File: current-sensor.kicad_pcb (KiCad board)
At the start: 2 copper layers, 78 x 39.3 mm, 36 parts, among them J1 ‎0197134001‎, J2 ‎0197134001‎, J3 0731000105, J4 Molex_SL_01x02_Male, J5 Molex_SL_01x02_Male, SW1 PN12SHNA03QE, SW2 OS103011MA7QP1, SW3 OS103011MA7QP1, U1 ACS730xLCTR-40AB, U2 AD8616xRM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

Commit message: swap 100kHz and 1kHz bandwidth positions
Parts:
- moved C1 4.00 mm to (148.0, 98.0)
- moved C3 4.00 mm to (144.0, 98.0)
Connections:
- SW3 pad 2: Net-(C1-Pad2) -> Net-(C3-Pad2)
- SW3 pad 4: Net-(C3-Pad2) -> Net-(C1-Pad2)
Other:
- board text added: "Current Sensor r0 G. Keeth github.com/gkeeth/current-sensor 2020-10-17"
- board text removed: "Current Sensor r0 G. Keeth github.com/gkeeth/current-sensor 2020-08-13"

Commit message: update pcb with hall effect sensor PN change
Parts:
- U1: value ACS730xLCTR-40AB -> ACS730xLCTR-20AB

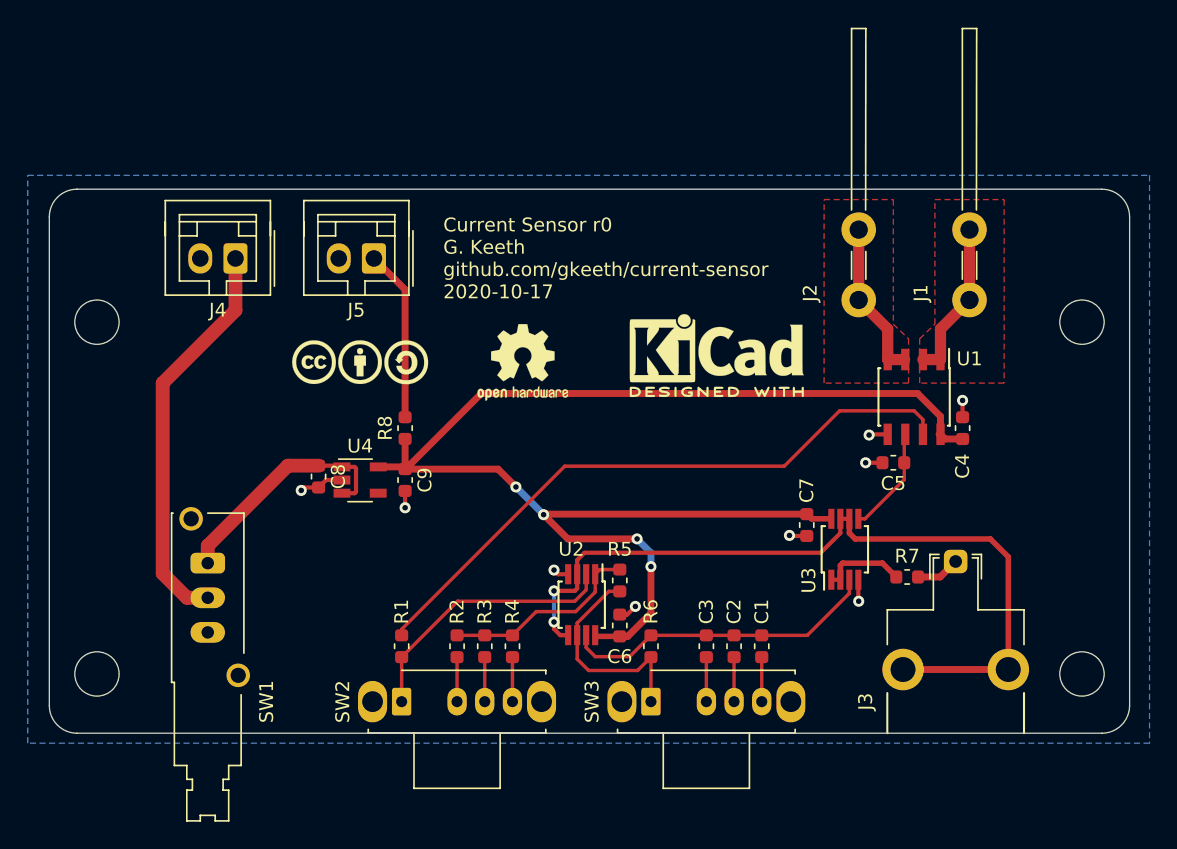
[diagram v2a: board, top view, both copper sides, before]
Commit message: adjust planes around current connectors and add silk
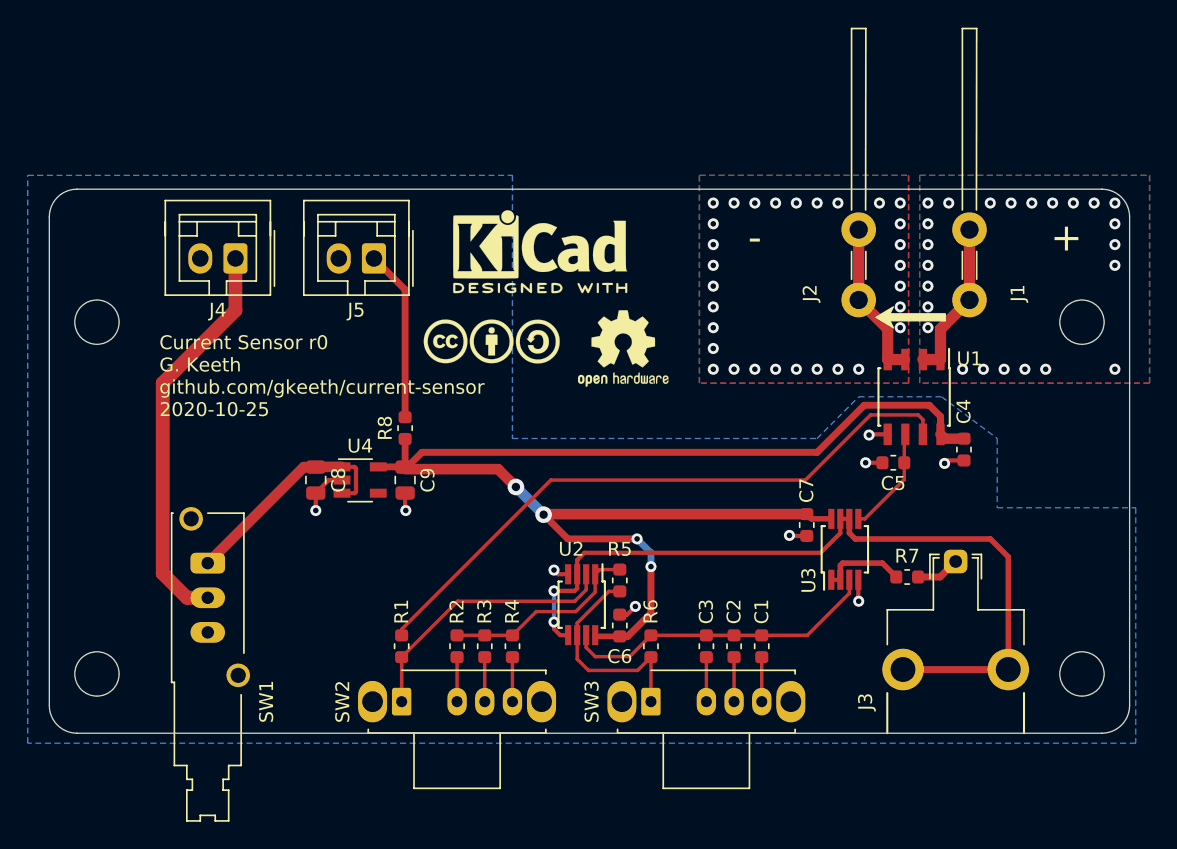
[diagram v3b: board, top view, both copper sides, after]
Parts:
- C8, C9: footprint Capacitor_SMD:C_0603_1608Metric -> Capacitor_SMD:C_0805_2012Metric
- R8: value R -> 3.3k
- moved LOGO2 14.8 mm to (132.0, 69.5)
- moved LOGO1 9.62 mm to (128.5, 76.0)
- moved LOGO3 7.32 mm to (138.0, 76.5)
- moved C4 1.55 mm to (162.6, 83.8), turned to 90 degrees
- moved C8 0.32 mm to (115.8, 86.0)
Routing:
- net /9V_switched: track 17.2 -> 18.1 mm
- net GND: track 13.6 -> 14.2 mm
- net +5V: track 99.2 -> 98.6 mm
- net /current-: vias 0 -> 30
- net /current+: vias 0 -> 23
- net (no net): vias 0 -> 1
- added copper zone on B.Cu, net /current+
- added copper zone on B.Cu, net /current-
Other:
- board text added: "+"
- board text added: "-"
- board text added: "Current Sensor r0 G. Keeth github.com/gkeeth/current-sensor 2020-10-25"
- board text removed: "Current Sensor r0 G. Keeth github.com/gkeeth/current-sensor 2020-10-17"

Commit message: decrease solder mask clearance to 0 as recommended
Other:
- rule pad_to_mask_clearance: 0.05 -> 0

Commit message: add JLC order number silk
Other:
- board text added: "JLCJLCJLCJLC"

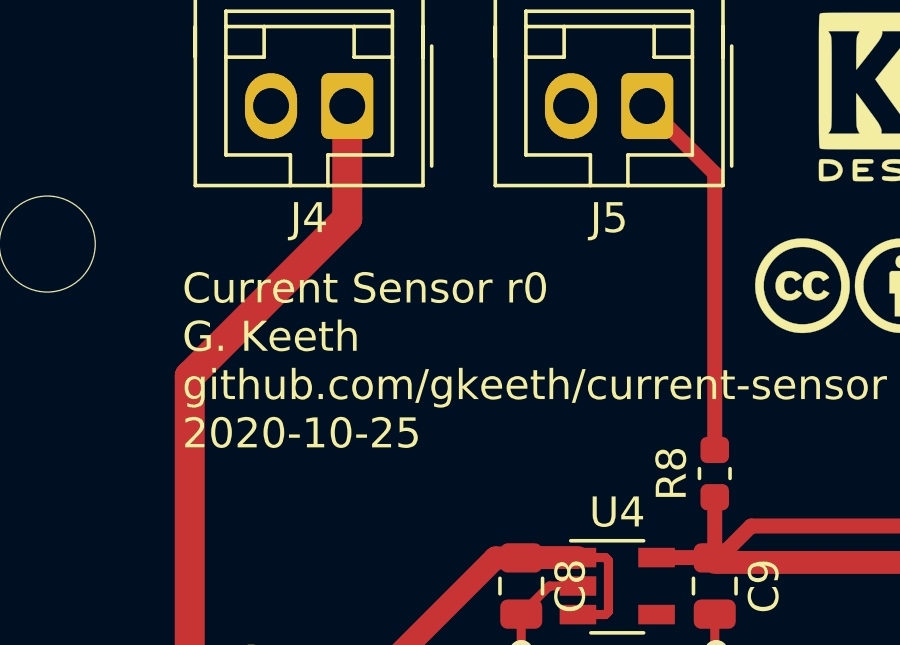
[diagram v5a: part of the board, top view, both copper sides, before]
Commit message: add fab/silk polarity marks to led/power connectors
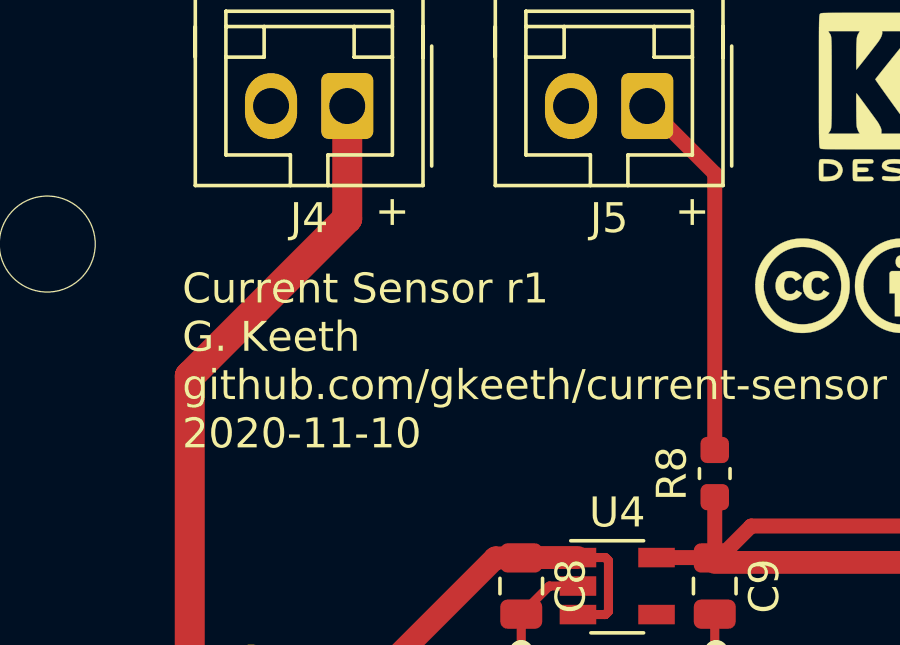
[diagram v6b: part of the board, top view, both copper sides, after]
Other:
- board text added: "Current Sensor r1 G. Keeth github.com/gkeeth/current-sensor 2020-11-10"
- board text removed: "Current Sensor r0 G. Keeth github.com/gkeeth/current-sensor 2020-10-25"
